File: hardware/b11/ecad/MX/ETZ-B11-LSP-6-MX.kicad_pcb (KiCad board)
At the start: 2 copper layers, 144.7 x 90.2 mm, 339 parts

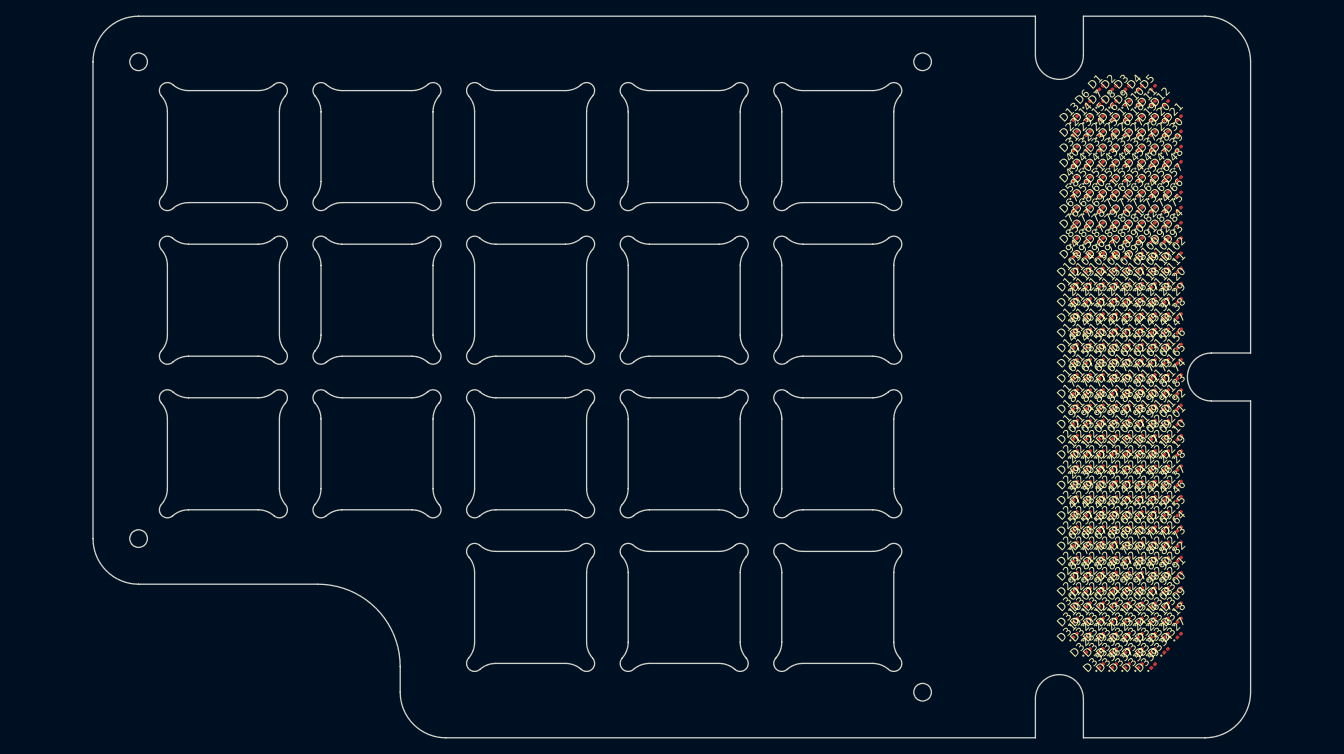
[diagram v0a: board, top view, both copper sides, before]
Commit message: refactor(hardware/b11): restructure ecad + tools, add KS-33 boards
- Rename PCB files: *-N → *-MX, *-L → *-CHOC-V2
- Reorganise ecad/ into per-family subfolders (MX/, CHOC-V2/, KS-33/)
- Add 8 blank KS-33 boards (outline only, human-populated ad-hoc)
- Apply JLCPCB-validated stackup (white/black/FR4 natural/black/white)
  to all 24 boards; SP boards at correct family thickness
- Add hardware/b11/tools/: config.py, placement.py, place-switch-sockets.py,
  place-switch-leds.py, place-display-leds.py — family-aware, non-destructive
- Archive old placement + generation scripts to hardware/scripts/_archive/
- Remove switch-origins.yaml (replaced by GRID_ORIGINS in config.py)
- Add PLAN.md tracking refactor progress

Co-Authored-By: Claude Sonnet 4.6 <noreply@anthropic.com>
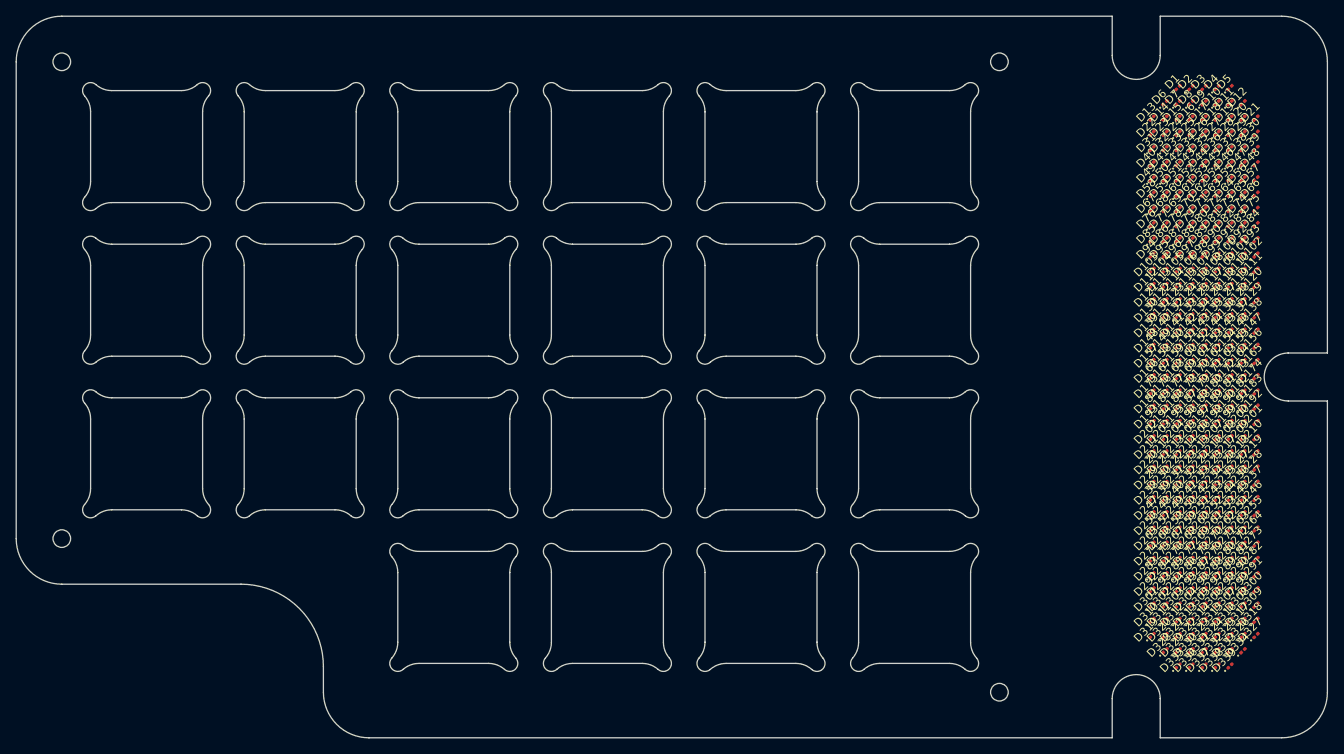
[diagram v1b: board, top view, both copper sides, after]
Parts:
- moved D1 9.60 mm to (211.8, 68.1)
- moved D10 9.60 mm to (216.7, 70.0)
- moved D100 9.60 mm to (218.3, 89.1)
- moved D101 9.60 mm to (219.9, 89.1)
- moved D102 9.60 mm to (221.5, 89.1)
- moved D103 9.60 mm to (208.5, 91.0)
- moved D104 9.60 mm to (210.2, 91.0)
- moved D105 9.60 mm to (211.8, 91.0)
- moved D106 9.60 mm to (213.4, 91.0)
- moved D107 9.60 mm to (215.0, 91.0)
- moved D108 9.60 mm to (216.7, 91.0)
- moved D109 9.60 mm to (218.3, 91.0)
- moved D11 9.60 mm to (218.3, 70.0)
- moved D110 9.60 mm to (219.9, 91.0)
- moved D111 9.60 mm to (221.5, 91.0)
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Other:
- board size 144.7 x 90.2 mm -> 163.9 x 90.2 mm
